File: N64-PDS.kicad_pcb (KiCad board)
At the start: 4 copper layers, 35.5 x 59.8 mm, 37 parts, among them J1 PWR_OUT, J2 I2C_OUT, J3 USB-C-6P-PWR, U2 ST1S41PHR, U3 STL6P3LLH6, U4 STUSB4500QTR

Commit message: Update board
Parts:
- removed CR3: ESDA25P35-1U1M, ESDA25P35:QFN1610_STM-M
- removed G***: LOGO, LOGO
- removed REF** (x4): MountingHole_2.2mm_M2_DIN965_Pad, MountingHole:MountingHole_2.2mm_M2_DIN965_Pad
- added C1: 1u, Capacitor_SMD:C_0402_1005Metric_Pad0.74x0.62mm_HandSolder, F.Cu at (197.0, 84.7)
- added C13: 1u, Capacitor_SMD:C_0402_1005Metric_Pad0.74x0.62mm_HandSolder, F.Cu at (147.8, 113.0)
- added C14: 1u, Capacitor_SMD:C_0402_1005Metric_Pad0.74x0.62mm_HandSolder, F.Cu at (149.8, 113.2)
- added C15: 1u, Capacitor_SMD:C_0402_1005Metric_Pad0.74x0.62mm_HandSolder, F.Cu at (150.8, 113.2)
- added C16: 27u, Capacitor_SMD:CP_Elec_5x5.9, F.Cu at (157.8, 79.0)
- added C17: 1u, Capacitor_SMD:C_0402_1005Metric_Pad0.74x0.62mm_HandSolder, F.Cu at (197.0, 92.6)
- added C18: 220u, Capacitor_SMD:CP_Elec_6.3x5.9, F.Cu at (141.5, 79.2)
- added C19: 47u, Capacitor_SMD:C_0805_2012Metric_Pad1.18x1.45mm_HandSolder, F.Cu at (185.4, 85.2)
- added C20: 100n, Capacitor_SMD:C_0504_1310Metric_Pad0.83x1.28mm_HandSolder, F.Cu at (147.2, 106.0)
- added C21: 47u, Capacitor_SMD:C_0805_2012Metric_Pad1.18x1.45mm_HandSolder, F.Cu at (185.4, 88.2)
- added C22: 47u, Capacitor_SMD:C_0805_2012Metric_Pad1.18x1.45mm_HandSolder, F.Cu at (185.4, 91.2)
- added C23: 100n, Capacitor_SMD:C_0402_1005Metric_Pad0.74x0.62mm_HandSolder, F.Cu at (197.0, 94.5)
- added C24: 100n, Capacitor_SMD:C_0603_1608Metric_Pad1.08x0.95mm_HandSolder, F.Cu at (186.5, 116.2)
- added C25: 100n, Capacitor_SMD:C_0603_1608Metric_Pad1.08x0.95mm_HandSolder, F.Cu at (184.0, 107.2)
- added C26: 1u, Capacitor_SMD:C_0603_1608Metric_Pad1.08x0.95mm_HandSolder, F.Cu at (190.0, 95.0)
- added C27: 4.7u, Capacitor_SMD:C_0603_1608Metric_Pad1.08x0.95mm_HandSolder, F.Cu at (190.0, 97.5)
- added C28: 27u, Capacitor_SMD:C_Elec_5x5.8, F.Cu at (139.5, 101.8)
- added C29: 10u, Capacitor_SMD:C_1210_3225Metric_Pad1.33x2.70mm_HandSolder, F.Cu at (184.2, 101.2)
- added C30: 1u, Capacitor_SMD:C_0402_1005Metric_Pad0.74x0.62mm_HandSolder, F.Cu at (197.0, 96.5)
- added C7: 100n, Capacitor_SMD:C_0603_1608Metric_Pad1.08x0.95mm_HandSolder, F.Cu at (190.0, 85.0)
- added C8: 1u, Capacitor_SMD:C_0603_1608Metric_Pad1.08x0.95mm_HandSolder, F.Cu at (190.0, 87.5)
- added L2: 5.2u, Inductor_SMD:L_Coilcraft_XAL6060-XXX, F.Cu at (185.0, 111.8)
- added R10: 100k, Resistor_SMD:R_0402_1005Metric_Pad0.72x0.64mm_HandSolder, F.Cu at (154.2, 119.5)
- added R15: 100, Resistor_SMD:R_0402_1005Metric_Pad0.72x0.64mm_HandSolder, F.Cu at (147.0, 108.5)
- added R16: 1k, Resistor_SMD:R_0402_1005Metric_Pad0.72x0.64mm_HandSolder, F.Cu at (149.5, 108.2)
- added R17: 56.2k, Resistor_SMD:R_0402_1005Metric_Pad0.72x0.64mm_HandSolder, F.Cu at (193.8, 92.7)
- added R18: 48.7k, Resistor_SMD:R_0402_1005Metric_Pad0.72x0.64mm_HandSolder, F.Cu at (193.8, 94.6)
- added R19: 100k, Resistor_SMD:R_0402_1005Metric_Pad0.72x0.64mm_HandSolder, F.Cu at (193.8, 96.6)
- added R20: 274, Resistor_SMD:R_0402_1005Metric_Pad0.72x0.64mm_HandSolder, F.Cu at (193.8, 98.6)
- added R8: 100k, Resistor_SMD:R_0402_1005Metric_Pad0.72x0.64mm_HandSolder, F.Cu at (152.2, 122.0)
- added U1: STUSB4500QTR, STUSB4500:QFN24EP_4X4_STM-M, F.Cu at (150.5, 117.5)
- C10, C11: value 1u -> 4.7u; footprint Capacitor_SMD:C_0402_1005Metric_Pad0.74x0.62mm_HandSolder -> Capacitor_SMD:C_0805_2012Metric_Pad1.18x1.45mm_HandSolder
- C2: footprint Capacitor_SMD:C_0805_2012Metric_Pad1.18x1.45mm_HandSolder -> Capacitor_SMD:C_1210_3225Metric_Pad1.33x2.70mm_HandSolder
- C3: value 10u -> 47u; footprint Capacitor_SMD:C_0603_1608Metric -> Capacitor_SMD:C_Elec_6.3x5.8
- C4: value 100n -> 4.7u; footprint Capacitor_SMD:C_0504_1310Metric -> Capacitor_SMD:C_0603_1608Metric_Pad1.08x0.95mm_HandSolder
- C5: value 10u -> 4.7u; footprint Capacitor_SMD:C_0603_1608Metric_Pad1.08x0.95mm_HandSolder -> Capacitor_SMD:C_0805_2012Metric_Pad1.18x1.45mm_HandSolder
- C6: value 1u -> 100n; footprint Capacitor_SMD:C_0402_1005Metric_Pad0.74x0.62mm_HandSolder -> Capacitor_SMD:C_0603_1608Metric_Pad1.08x0.95mm_HandSolder
- C9: value 1u -> 100n
- CR1: value ESDA25P35-1U1M -> ESDA25W; footprint ESDA25P35:QFN1610_STM-M -> ESDA25W:SOT323-3L_STM-M
- CR2: value ESDA25W -> ESDA25P35-1U1M; footprint ESDA25W:SOT323-3L_STM-M -> ESDA25P35:QFN1610_STM-M
- J1: value PWR_OUT -> USB-C-6P-PWR; footprint Connector_JST:JST_NV_B04P-NV_1x04_P5.00mm_Vertical -> Connector_USB:USB_C_Receptacle_GCT_USB4125-xx-x-0190_6P_TopMnt_Horizontal
- J2: footprint Connector_Wire:SolderWire-1.5sqmm_1x03_P6mm_D1.7mm_OD3mm -> Connector_Molex:Molex_PicoBlade_53047-0410_1x04_P1.25mm_Vertical
- J3: value USB-C-6P-PWR -> PWR_OUT; footprint Connector_USB:USB_C_Receptacle_GCT_USB4125-xx-x-0190_6P_TopMnt_Horizontal -> Connector_JST:JST_NV_B04P-NV_1x04_P5.00mm_Vertical
- L1: value 2.5u -> 10u; footprint Inductor_SMD:L_Coilcraft_MSS1048-XXX -> Library:DR1040-5R2-R
- R1: value 75k -> 274k
- R11: value 1k -> 22K
- R12: value 10k -> 470
- R13: value 100k -> 1k
- R2: value 1k -> 100k
- R3: value 0 -> 10k
- R4: value 470 -> 100k
- R5: value 24k -> 0
- R6: value 100k -> 50k
- R7: value 100 -> 48.7k
- R9: value 22K -> 301
- U2: value ST1S41PHR -> PTPS55289RYQR; footprint ST1S41PHR:HSOP8_STM-M -> PTPS55289RYQR:RYQ0021A-MFG
- U3: footprint STL6P3LLH6:POWERFLAT_3P3X3P3_STM-M -> STL6P3LLH6:POWERFLAT_3P3X3P3_STM
- U4: value STUSB4500QTR -> PTPS55289RYQR; footprint STUSB4500:QFN24EP_4X4_STM-M -> PTPS55289RYQR:RYQ0021A-MFG
- moved L1 72.7 mm to (213.8, 78.2), turned to -90 degrees
- moved C10 72.0 mm to (198.0, 65.2), turned to 0 degrees
- moved C5 69.9 mm to (198.0, 62.2), turned to 0 degrees
- moved C11 69.1 mm to (198.0, 68.2), turned to 0 degrees
- moved C12 65.5 mm to (198.0, 71.2), turned to 0 degrees
- moved C6 63.9 mm to (193.0, 72.6), turned to 0 degrees
- moved C2 60.5 mm to (199.5, 48.7), turned to 0 degrees
- moved C9 54.3 mm to (183.6, 71.4), turned to 0 degrees
- moved CR2 53.8 mm to (176.6, 72.0)
- moved C4 53.4 mm to (193.0, 70.1), turned to 0 degrees
- moved R2 53.2 mm to (175.7, 65.5), turned to 0 degrees
- moved R6 51.5 mm to (178.9, 65.5), turned to 0 degrees
- moved J1 51.2 mm to (137.5, 117.5), turned to -90 degrees
- moved R9 50.1 mm to (178.9, 69.4), turned to 0 degrees
- moved R1 48.8 mm to (175.7, 63.5), turned to 0 degrees
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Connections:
- C10 pad 1: 2V7 -> GND
- C10 pad 2: GND -> 12VO
- C11 pad 1: Net-(U4-VREG_1V2) -> GND
- C11 pad 2: GND -> 12VO
- C12 pad 1: /VBUS -> GND
- C12 pad 2: GND -> 12VO
- C2 pad 1: 3V3O -> VSNK
- C4 pad 1: /VBUS_EN_SNK -> GND
- C4 pad 2: VSNK -> Net-(U2-VCC)
- C5 pad 1: GND -> /VBUS
- C5 pad 2: VSNK -> GND
- C6 pad 1: /VBUS -> Net-(U2-BOOT1)
- C6 pad 2: GND -> Net-(U2-SW1)
- C9 pad 1: GND -> Net-(U2-COMP)
- C9 pad 2: /VBUS_VS_DISCH -> Net-(C9-Pad2)
- CR1 pad 1: VSNK -> Net-(J1-CC1)
- CR1 pad 2: GND -> Net-(J1-CC2)
- CR2 pad 1: Net-(J3-CC1) -> /VBUS
- CR2 pad 2: Net-(J3-CC2) -> GND
- J2 pad 2: /I2C_SDA -> I2C_SCL
- J2 pad 3: /I2C_SCL -> I2C_SDA
- L1 pad 1: /3V3_SWO -> Net-(U2-SW1)
- L1 pad 2: 3V3O -> Net-(U2-SW2)
- R1 pad 1: 3V3O -> VSNK
- R1 pad 2: 3V3FB -> Net-(U2-EN_UVLO)
- R11 pad 1: DISCH -> Net-(U1-VBUS_EN_SNK)
- R11 pad 2: VSNK -> Net-(U3-G)
- R12 pad 1: GND -> /VBUS
- R12 pad 2: Net-(U4-RESET) -> /VBUS_VS_DISCH
- R13 pad 1: Net-(U4-ADDR0) -> /VBUS_VS_DISCH
- R13 pad 2: GND -> Net-(U1-VBUS_VS_DISCH)
- R14 pad 1: /ADDR1 -> /VBUS
- R14 pad 2: GND -> Net-(U3-G)
- R2 pad 1: /VBUS_VS_DISCH -> GND
- R2 pad 2: Net-(U4-VBUS_VS_DISCH) -> Net-(U2-EN_UVLO)
- R3 pad 1: Net-(U4-ADDR0) -> GND
- R3 pad 2: 2V7 -> Net-(U1-RESET)
- R4 pad 1: /VBUS -> GND
- R4 pad 2: /VBUS_VS_DISCH -> Net-(U2-VCC)
- R5 pad 1: 3V3FB -> Net-(U1-ADDR0)
- R5 pad 2: GND -> 2V7
- R6 pad 1: /VBUS -> Net-(U2-MODE)
- R6 pad 2: Net-(U3-G) -> Net-(U2-VCC)
- R7 pad 1: Net-(U3-G) -> Net-(U2-FSW)
- R7 pad 2: /VBUS_EN_SNK -> GND
- R9 pad 1: Net-(U4-VBUS_EN_SNK) -> GND
- R9 pad 2: Net-(U3-G) -> Net-(C9-Pad2)
- U2 pad 1: VSNK -> Net-(U2-EN_UVLO)
- U2 pad 2: VSNK -> Net-(U2-MODE)
- U2 pad 3: 3V3FB -> I2C_SCL
- U2 pad 4: GND -> I2C_SDA
- U2 pad 5: unconnected-(U2-NC-Pad5) -> GND
- U2 pad 6: VSNK -> Net-(U2-FSW)
- U2 pad 7: /3V3_SWO -> VSNK
- U2 pad 8: GND -> Net-(U2-SW1)
- U4 pad 1: Net-(J3-CC1) -> Net-(U4-EN_UVLO)
- U4 pad 10: GND -> Net-(U4-SW2)
- U4 pad 11: unconnected-(U4-ATTACH-Pad11) -> 3V3O
- U4 pad 12: Net-(U4-ADDR0) -> 3V3O
- U4 pad 13: /ADDR1 -> 3V3O
- U4 pad 15: unconnected-(U4-GPIO-Pad15) -> Net-(U4-COMP)
- U4 pad 16: Net-(U4-VBUS_EN_SNK) -> unconnected-(U4-CDC-Pad16)
- U4 pad 17: unconnected-(U4-A_B_SIDE-Pad17) -> GND
- U4 pad 18: Net-(U4-VBUS_VS_DISCH) -> Net-(U4-VCC)
- U4 pad 19: unconnected-(U4-ALERT-Pad19) -> Net-(U4-BOOT2)
- U4 pad 2: Net-(J3-CC1) -> GND
- U4 pad 20: unconnected-(U4-POWER_OK2-Pad20) -> Net-(U4-BOOT1)
- U4 pad 21: Net-(U4-VREG_1V2) -> unconnected-(U4-EXTVCC-Pad21)
- U4 pad 3: unconnected-(U4-NC-Pad3) -> I2C_SCL
- U4 pad 4: Net-(J3-CC2) -> I2C_SDA
- U4 pad 5: Net-(J3-CC2) -> GND
- U4 pad 6: Net-(U4-RESET) -> Net-(U4-FSW)
- U4 pad 7: /I2C_SCL -> VSNK
- U4 pad 8: /I2C_SDA -> Net-(U4-SW1)
- U4 pad 9: DISCH -> GND
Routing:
- net 3V3O: track 29.3 -> 0.00 mm, vias 2 -> 0
- net DISCH: track 1.79 -> 24.3 mm
- net GND: track 59.9 -> 40.1 mm, vias 21 -> 7
- net VSNK: track 50.4 -> 30.7 mm
- net Net-(J3-CC2): track 17.9 -> 0.00 mm, vias 2 -> 0
- net /I2C_SDA: track 17.8 -> 0.00 mm
- net Net-(J3-CC1): track 15.7 -> 0.00 mm, vias 2 -> 0
- net I2C_SCL: track 0.00 -> 14.3 mm
- net I2C_SDA: track 0.00 -> 14.3 mm
- net /I2C_SCL: track 12.8 -> 0.00 mm
- net Net-(J1-CC2): track 0.00 -> 10.9 mm
- net Net-(J1-CC1): track 0.00 -> 10.0 mm
- net Net-(U3-G): track 9.16 -> 15.0 mm
- net /VBUS: track 41.4 -> 36.4 mm, vias 2 -> 0
- net /3V3_SWO: track 4.09 -> 0.00 mm
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- removed copper zone on F.Cu, net 3V3O
- removed copper zone on In1.Cu, net GND

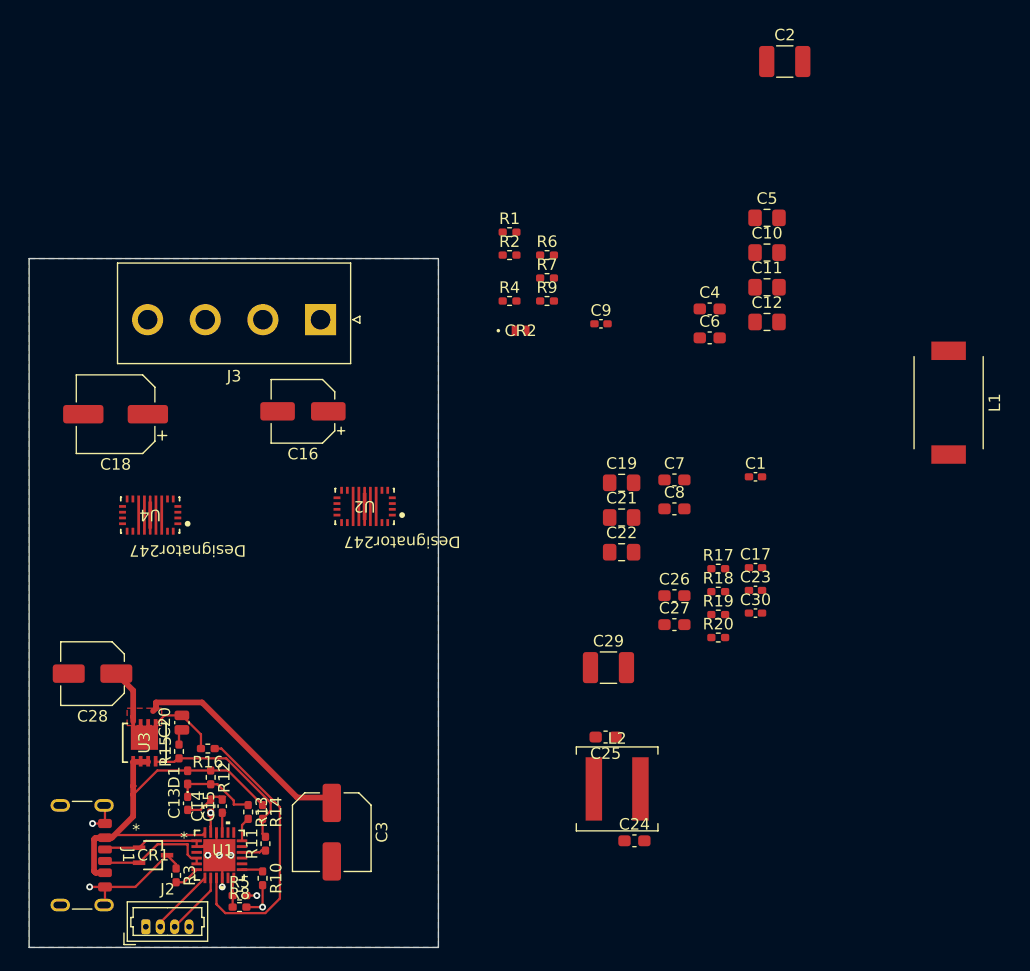
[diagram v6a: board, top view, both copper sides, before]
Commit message: Finish board layout and routing
Finished board layout and routing, added a hatched ground plane for looks (and some emi)
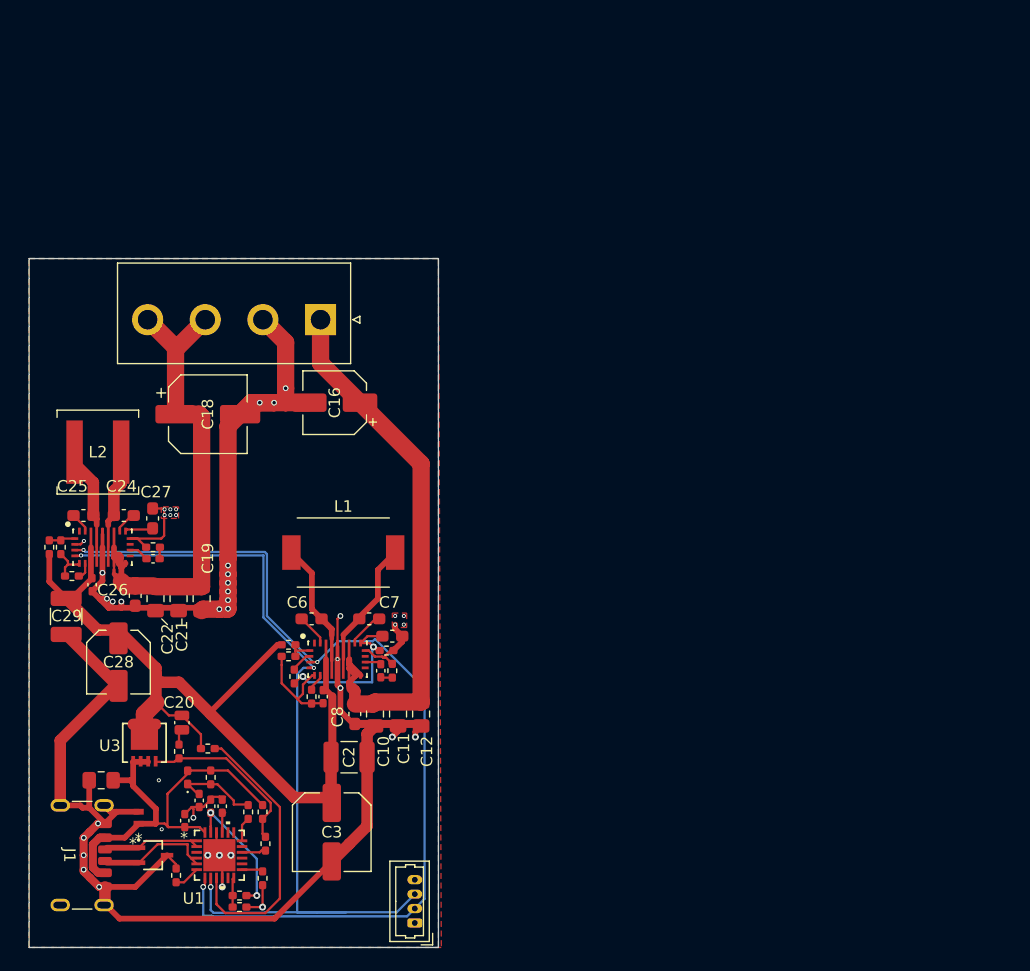
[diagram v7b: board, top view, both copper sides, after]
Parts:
- moved C5 75.6 mm to (140.2, 111.0), turned to 180 degrees
- moved C2 71.2 mm to (161.8, 109.0)
- moved R20 58.5 mm to (135.8, 90.8), turned to 90 degrees
- moved C30 57.6 mm to (139.5, 94.0), turned to -90 degrees
- moved R19 57.3 mm to (136.8, 90.8), turned to 90 degrees
- moved R18 56.1 mm to (137.7, 93.3), turned to 180 degrees
- moved C17 54.1 mm to (147.5, 114.5), turned to 90 degrees
- moved L1 54.1 mm to (161.2, 91.2), turned to 0 degrees
- moved CR2 53.7 mm to (143.5, 114.2), turned to 90 degrees
- moved L2 53.7 mm to (140.0, 82.5)
- moved C10 52.5 mm to (164.0, 105.2), turned to 90 degrees
- moved C24 52.5 mm to (142.2, 88.0), turned to 180 degrees
- moved C23 52.3 mm to (144.8, 91.8), turned to 180 degrees
- moved C25 49.2 mm to (138.7, 88.0), turned to 0 degrees
- moved R17 49.1 mm to (144.8, 90.8)
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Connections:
- C23 pad 1: Net-(U4-COMP) -> Net-(C23-Pad1)
- C23 pad 2: Net-(C23-Pad2) -> Net-(U4-COMP)
- C7 pad 1: Net-(U2-BOOT2) -> Net-(U2-SW2)
- C7 pad 2: Net-(U2-SW2) -> Net-(U2-BOOT2)
- R17 pad 2: Net-(C23-Pad2) -> Net-(C23-Pad1)
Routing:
- net GND: track 40.1 -> 198.6 mm, vias 7 -> 43
- net I2C_SCL: track 14.3 -> 82.2 mm, vias 0 -> 3
- net I2C_SDA: track 14.3 -> 76.6 mm, vias 0 -> 3
- net 12VO: track 0.00 -> 52.4 mm
- net VSNK: track 30.7 -> 78.1 mm
- net 3V3O: track 0.00 -> 45.0 mm
- net Net-(U2-VCC): track 0.00 -> 14.4 mm, vias 0 -> 2
- net Net-(U2-SW2): track 0.00 -> 11.1 mm
- net Net-(U2-SW1): track 0.00 -> 10.7 mm
- net Net-(U4-SW2): track 0.00 -> 8.71 mm
- net Net-(U4-SW1): track 0.00 -> 8.32 mm
- net Net-(U2-BOOT2): track 0.00 -> 3.17 mm
- net Net-(U2-BOOT1): track 0.00 -> 2.77 mm
- net Net-(U4-VCC): track 0.00 -> 2.45 mm
- net Net-(U2-EN_UVLO): track 0.00 -> 2.25 mm
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- added copper zone on F.Cu, net GND
- removed copper zone on F.Cu, net VSNK
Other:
- copper layers 4 -> 2
